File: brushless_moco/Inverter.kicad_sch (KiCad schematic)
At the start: 0 parts

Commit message: Started inverter design
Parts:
- added Q1, Q2, Q3, Q4, Q5, Q6: IGC019S06S1, symbol brushless_moco_symbols:IGC019S06S1
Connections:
- new net: Q3.1 (D1), Q3.2 (D2)
- new net: Q3.4 (S1), Q3.5 (S2), Q3.6 (S3)
- new net: Q2.1 (D1), Q2.2 (D2)
- new net: Q2.4 (S1), Q2.5 (S2), Q2.6 (S3)
- new net: Q6.1 (D1), Q6.2 (D2)
- new net: Q6.4 (S1), Q6.5 (S2), Q6.6 (S3)
- new net: Q5.1 (D1), Q5.2 (D2)
- new net: Q5.4 (S1), Q5.5 (S2), Q5.6 (S3)
- new net: Q4.1 (D1), Q4.2 (D2)
- new net: Q4.4 (S1), Q4.5 (S2), Q4.6 (S3)
- new net: Q1.1 (D1), Q1.2 (D2)
- new net: Q1.4 (S1), Q1.5 (S2), Q1.6 (S3)

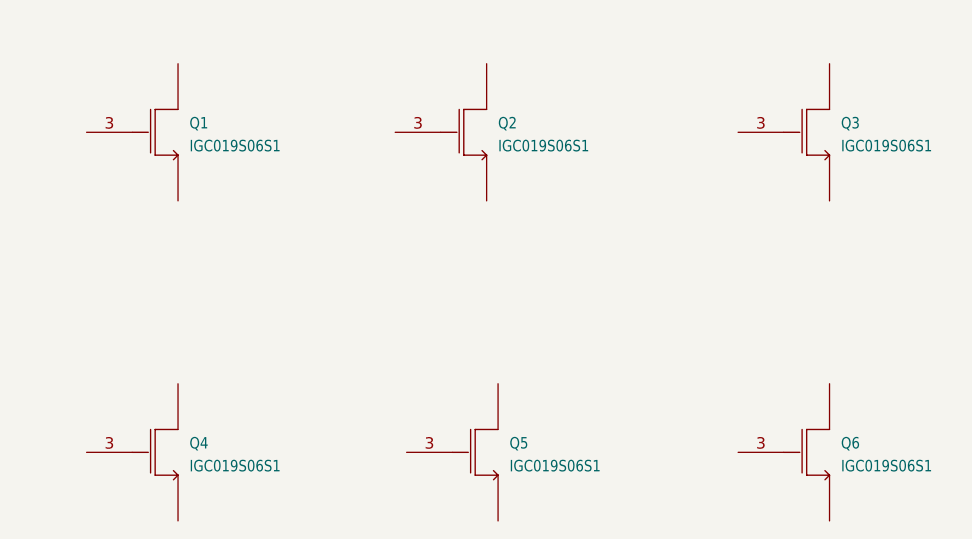
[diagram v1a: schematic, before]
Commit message: Switched fets
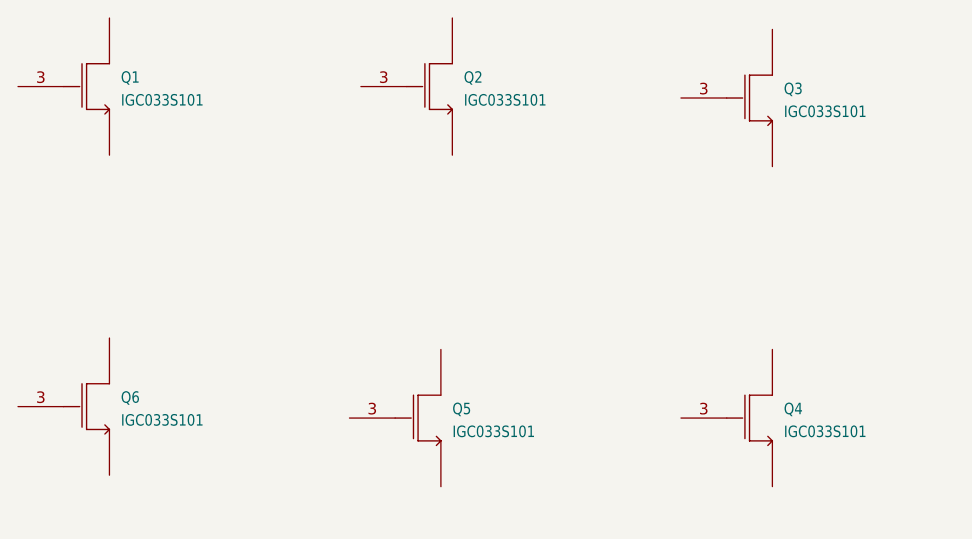
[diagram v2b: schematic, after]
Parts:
- removed Q1, Q2, Q3, Q4, Q5, Q6: IGC019S06S1, symbol brushless_moco_symbols:IGC019S06S1
- added Q1, Q2, Q3, Q4, Q5, Q6: IGC033S101, brushless_moco_footprints:IFX-PG-VSON-6-3-V, symbol brushless_moco_symbols:IGC033S101
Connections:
- new net: Q4.1 (D1), Q4.2 (D2)
- new net: Q4.4 (S1), Q4.5 (S2), Q4.6 (S3)
- new net: Q5.1 (D1), Q5.2 (D2)
- new net: Q5.4 (S1), Q5.5 (S2), Q5.6 (S3)
- new net: Q3.1 (D1), Q3.2 (D2)
- new net: Q3.4 (S1), Q3.5 (S2), Q3.6 (S3)
- new net: Q1.1 (D1), Q1.2 (D2)
- new net: Q1.4 (S1), Q1.5 (S2), Q1.6 (S3)
- new net: Q2.1 (D1), Q2.2 (D2)
- new net: Q2.4 (S1), Q2.5 (S2), Q2.6 (S3)
- new net: Q6.1 (D1), Q6.2 (D2)
- new net: Q6.4 (S1), Q6.5 (S2), Q6.6 (S3)

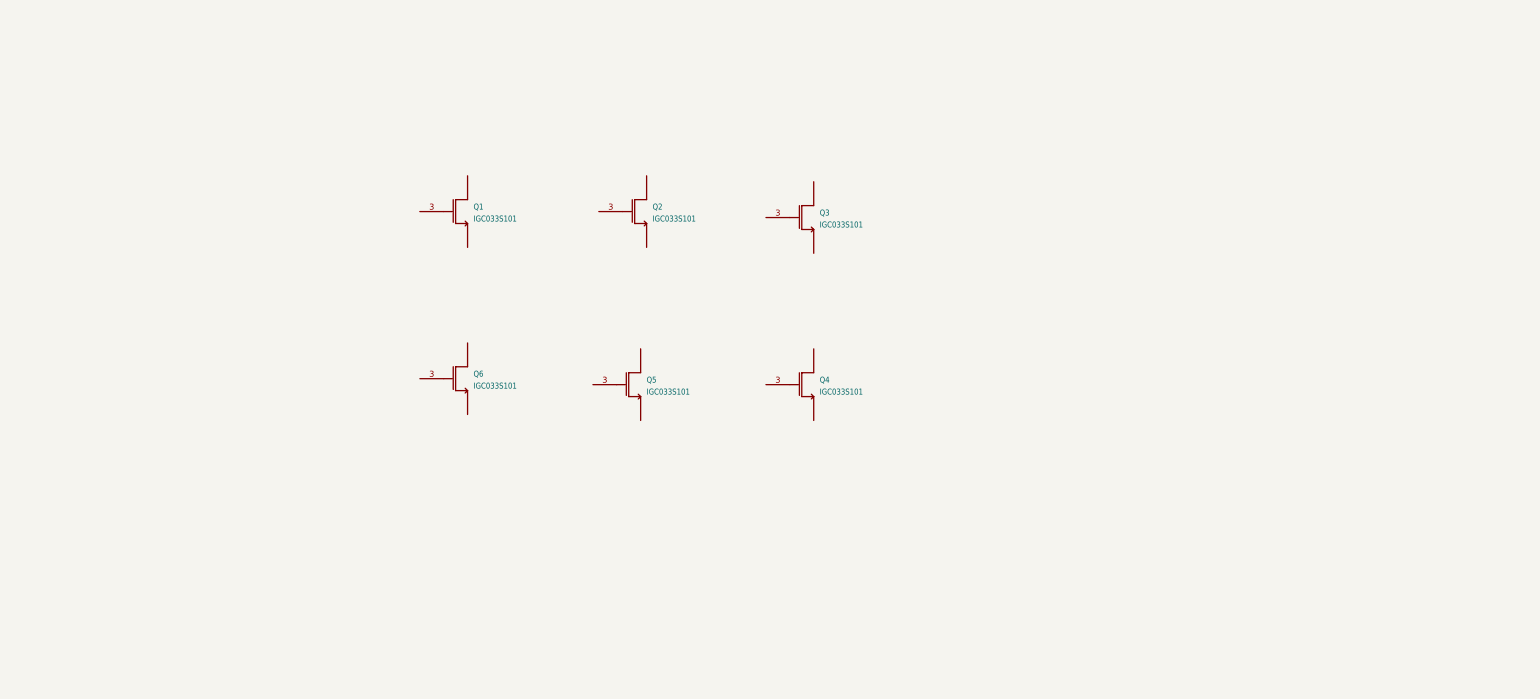
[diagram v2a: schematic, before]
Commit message: Added can transciever and current sensor symbols and libraries
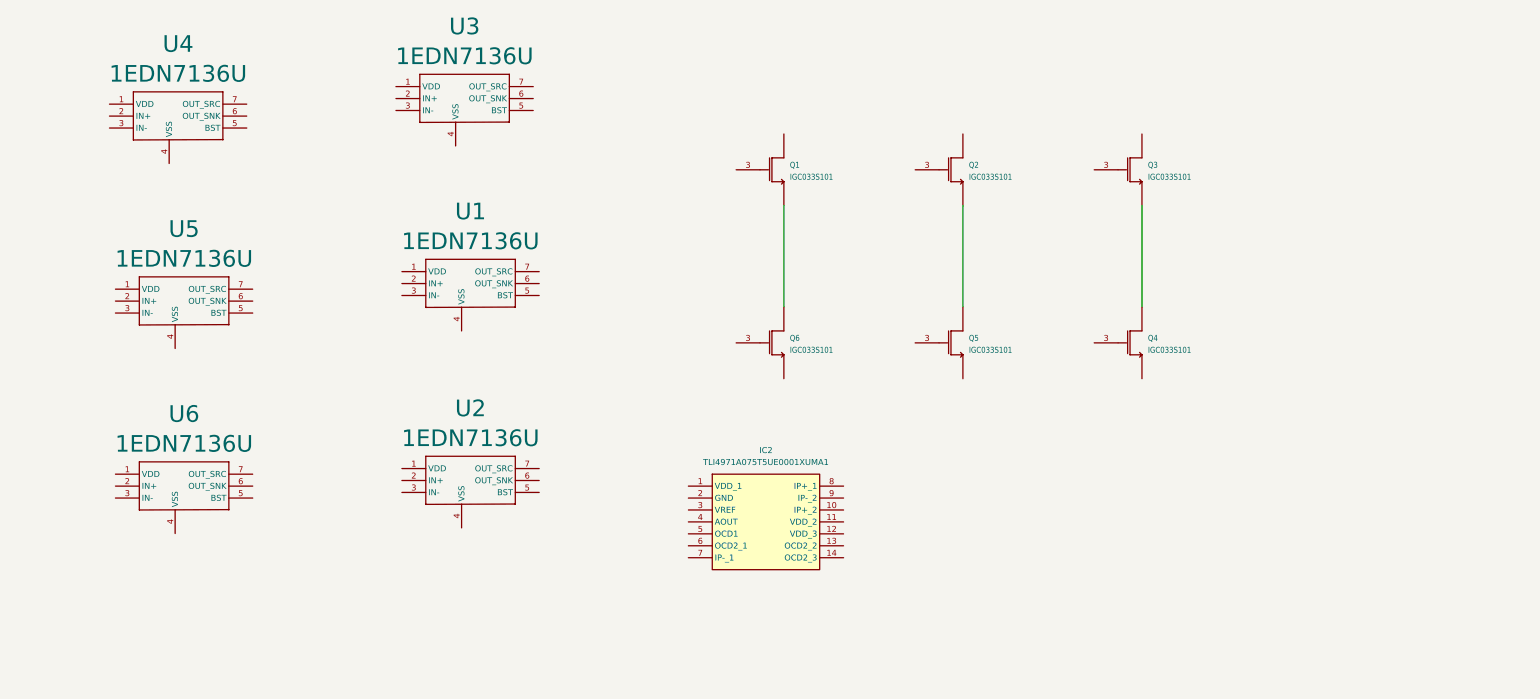
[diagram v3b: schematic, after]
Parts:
- added IC2: TLI4971A075T5UE0001XUMA1, brushless_moco_footprints:TLI4971A075T5UE0001XUMA1, symbol brushless_moco_symbols:TLI4971A075T5UE0001XUMA1
- added U1, U2, U3, U4, U5, U6: 1EDN7136U, symbol brushless_moco_symbols:1EDN7136U
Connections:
- net at Q4.1 (D1), Q4.2 (D2): now also Q3.4 (S1), Q3.5 (S2), Q3.6 (S3)
- net at Q5.1 (D1), Q5.2 (D2): now also Q2.4 (S1), Q2.5 (S2), Q2.6 (S3)
- net at Q1.4 (S1), Q1.5 (S2), Q1.6 (S3): now also Q6.1 (D1), Q6.2 (D2)
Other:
- moved on the sheet: Q1, Q2, Q3, Q4, Q5, Q6

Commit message: Added kicad workflow
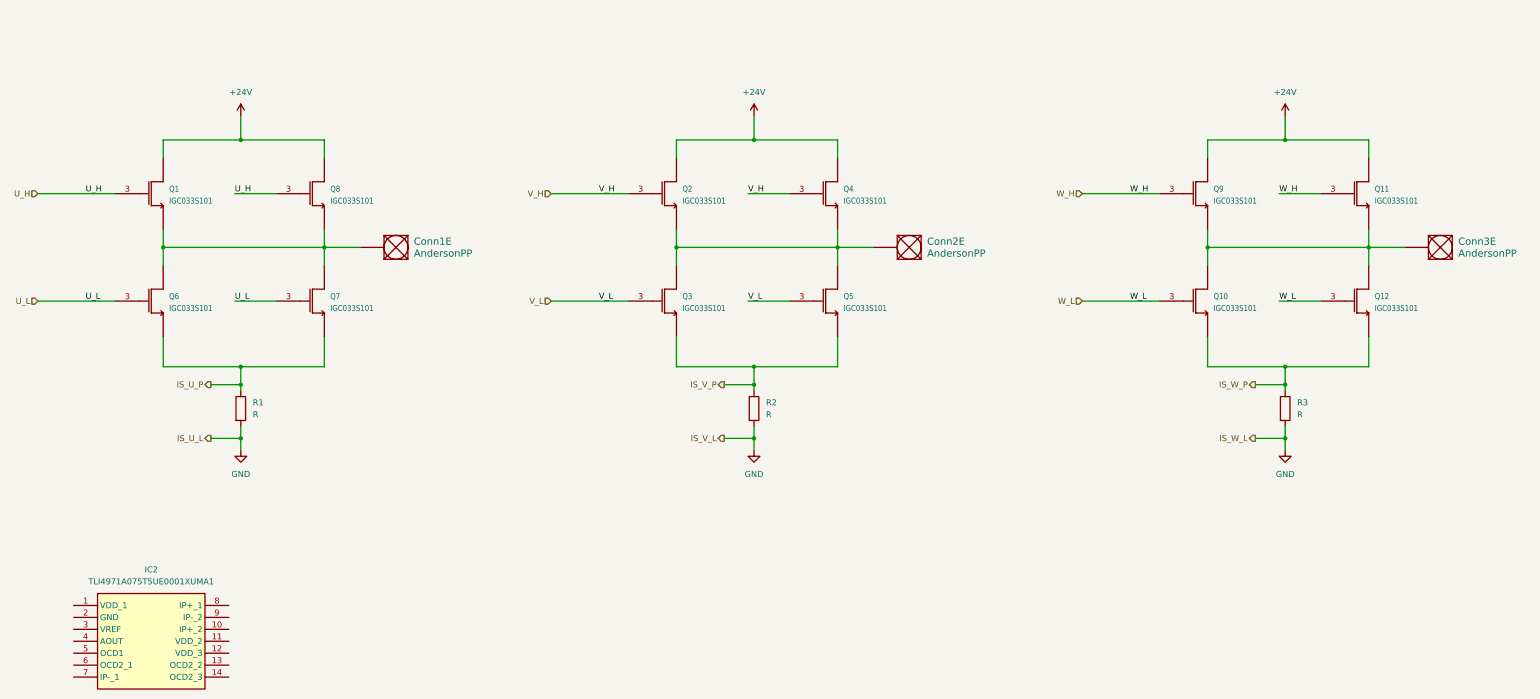
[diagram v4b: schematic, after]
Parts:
- removed U1, U2, U3, U4, U5, U6: 1EDN7136U, symbol brushless_moco_symbols:1EDN7136U
- added Conn1, Conn2, Conn3: AndersonPP, MRDT_Connectors:Square_Anderson_1_H, symbol MRDT_Connectors:AndersonPP
- added Q10, Q11, Q12, Q7, Q8, Q9: IGC033S101, brushless_moco_footprints:IFX-PG-VSON-6-3-V, symbol brushless_moco_symbols:IGC033S101
- added R1, R2, R3: R, symbol Device:R
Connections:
- net IS_V_P: now reaches Q3.4 (S1), Q3.5 (S2), Q3.6 (S3)
- net IS_V_P: now also Q5.4 (S1), Q5.5 (S2), Q5.6 (S3), R2.1; no longer Q4.1 (D1), Q4.2 (D2)
- net V_H: now reaches Q4.3 (G)
- net V_H: now also Q2.3 (G)
- net at Q4.4 (S1), Q4.5 (S2), Q4.6 (S3): now also Q2.4 (S1), Q2.5 (S2), Q2.6 (S3), Q3.1 (D1), Q3.2 (D2), Q5.1 (D1), Q5.2 (D2), Conn2.1
- net V_L: now reaches Q5.3 (G)
- net V_L: now also Q3.3 (G)
- net +24V: now reaches Q1.1 (D1), Q1.2 (D2)
- net +24V: now also Q2.1 (D1), Q2.2 (D2), Q4.1 (D1), Q4.2 (D2), Q11.1 (D1), Q11.2 (D2), Q8.1 (D1), Q8.2 (D2), Q9.1 (D1), Q9.2 (D2)
- net U_H: now reaches Q1.3 (G)
- net U_H: now also Q8.3 (G)
- net at Q1.4 (S1), Q1.5 (S2), Q1.6 (S3)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: now also Conn1.1, Q7.1 (D1), Q7.2 (D2), Q8.4 (S1), Q8.5 (S2), Q8.6 (S3)
- net U_L: now reaches Q6.3 (G)
- net U_L: now also Q7.3 (G)
- net IS_U_P: now reaches Q6.4 (S1), Q6.5 (S2), Q6.6 (S3)
- net IS_U_P: now also Q7.4 (S1), Q7.5 (S2), Q7.6 (S3), R1.1
- new net: Conn3.1, Q10.1 (D1), Q10.2 (D2), Q11.4 (S1), Q11.5 (S2), Q11.6 (S3), Q12.1 (D1), Q12.2 (D2), Q9.4 (S1), Q9.5 (S2), Q9.6 (S3)
- new net GND: R1.2, R2.2, R3.2
- new net IS_W_P: Q10.4 (S1), Q10.5 (S2), Q10.6 (S3), Q12.4 (S1), Q12.5 (S2), Q12.6 (S3), R3.1
- new net W_H: Q11.3 (G), Q9.3 (G)
- new net W_L: Q10.3 (G), Q12.3 (G)
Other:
- moved on the sheet: IC2, Q1, Q6
